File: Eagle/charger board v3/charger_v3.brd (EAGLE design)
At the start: 98.7 x 82.5 mm, 32 parts, among them IC1 IR2110D, Q1 2N7000, Q2 IRFP240, Q3 MJE13003G

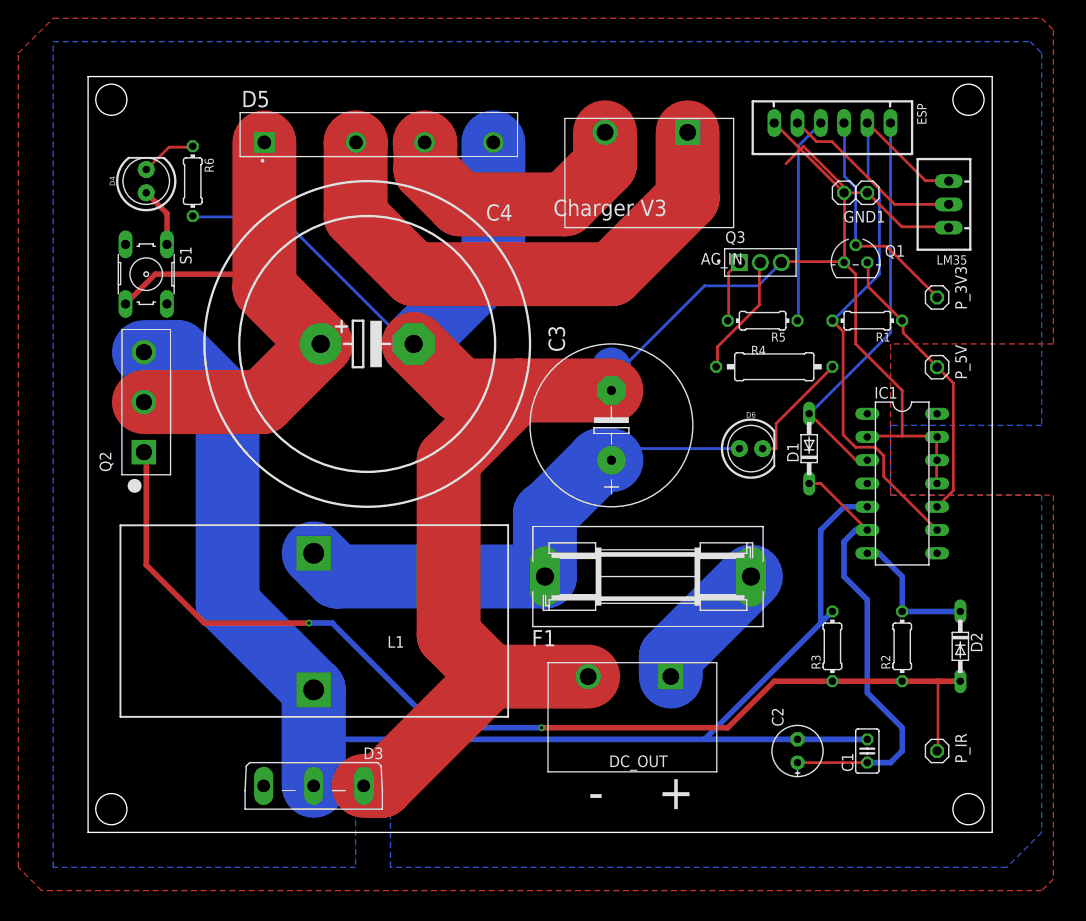
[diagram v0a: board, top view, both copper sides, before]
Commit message: ubah 2n700 ke opto + nambahin snubber di mosfet sama dioda
ubah 2n700 ke opto + nambahin snubber di mosfet sama dioda
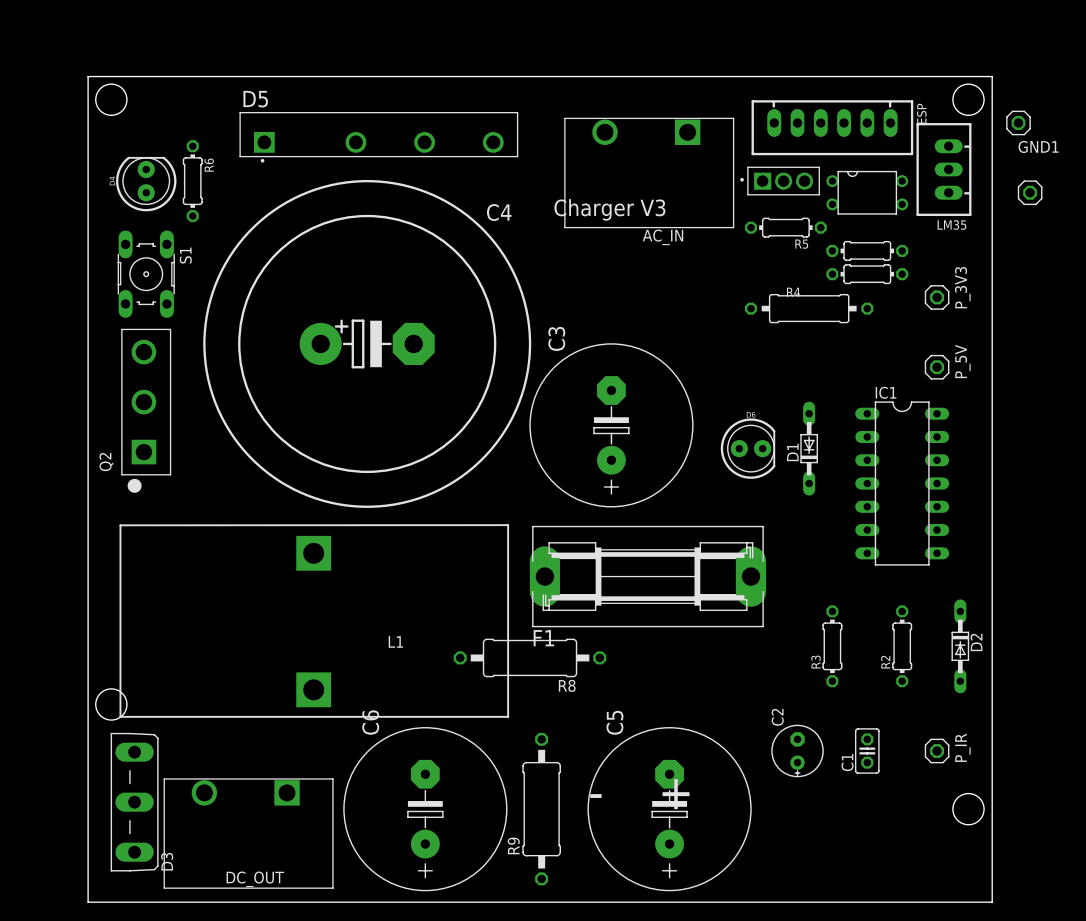
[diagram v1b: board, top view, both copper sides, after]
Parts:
- removed Q1: 2N7000, 2N7000:TO92
- added C5, C6: 22uF, rcl:E7,5-18
- added OK1: SFH618A-5, optocoupler:DIP4
- added R7: 1k, rcl:0204/7
- added R8, R9: 31, rcl:0411/15
- R1: value 10k -> 180
- moved DC_OUT 43.8 mm to (18.5, -1.02)
- moved D3 22.1 mm to (2.54, 3.30), turned to 90 degrees
- moved GND1 20.5 mm to (101.6, 77.5)
- moved GND2 17.8 mm to (102.9, 69.8)
- moved R5 10.5 mm to (76.2, 66.0)
- moved Q3 9.25 mm to (73.7, 71.1)
- moved R4 7.41 mm to (78.7, 57.2)
- moved R1 5.08 mm to (85.1, 61.0), turned to 0 degrees
- moved LM35 3.81 mm to (94.0, 72.4)
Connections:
- new net N$11: OK1.4, R1.2
- new net N$6: C5.+, R8.1
- new net N$7: C6.-, R9.2
- net 5V: now also R1.1; no longer R1.2
- net GND: now also C6.+, OK1.2, R7.1; no longer Q1.1
- net HVDC: now also R8.2
- net NMOS_SOURCE: now also C5.-, R9.1
- net PWM_5V: now also OK1.3, R7.2; no longer Q1.3, R1.1
- net PWM_SW1: now also OK1.1; no longer Q1.2
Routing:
- net GND: track 255.5 -> 0.00 mm
- net NMOS_SOURCE: track 157.3 -> 0.00 mm
- net PWM_12V: track 118.6 -> 0.00 mm, vias 2 -> 0
- net HVDC: track 72.3 -> 0.00 mm
- net 5V: track 64.7 -> 0.00 mm
- net AC_1: track 57.6 -> 0.00 mm
- net V_OUT: track 57.0 -> 0.00 mm
- net VB: track 49.5 -> 0.00 mm
- net 12V: track 43.9 -> 0.00 mm
- net PWM_5V: track 31.3 -> 0.00 mm
- net AC_2: track 29.5 -> 0.00 mm
- net PWM_SW1: track 25.2 -> 0.00 mm
- net PWM_SW2: track 22.7 -> 0.00 mm
- net TEMP: track 20.2 -> 0.00 mm
- net N$1: track 15.0 -> 0.00 mm
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- removed copper zone on layer 1, net GND
- removed copper zone on layer 16, net GND
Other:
- board size 98.7 x 82.5 mm -> 98.7 x 90.2 mm
